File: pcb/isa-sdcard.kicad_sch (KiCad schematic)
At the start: 34 parts, among them J1 SD Card Board, J3 Bus_ISA_8bit_AB_Rev0, SW1 ADDR SEL, U10 74HC32, U12 74HC165, U13 74HC595, U14 74HC00, U2 74HC00, U22 74HCT688, U4 74HC00, U5 74HC163, U6 74HCT138, U7 74HC123, U9 74HC32, X1 16MHz

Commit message: Revising schematics and layout
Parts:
- removed C1, C25, C5: 0.1uF, Capacitor_THT:C_Disc_D5.0mm_W2.5mm_P5.00mm, symbol Device:C
- removed C20, C21: 22pF, Capacitor_THT:C_Disc_D5.0mm_W2.5mm_P5.00mm, symbol Device:C
- removed J1: SD Card Board, sdcard-holder:sdcard-socket, symbol Connector:Conn_01x06_Female
- removed R3: 10k, Resistor_THT:R_Axial_DIN0207_L6.3mm_D2.5mm_P7.62mm_Horizontal, symbol Device:R
- removed R5: 1k, Resistor_THT:R_Axial_DIN0207_L6.3mm_D2.5mm_P7.62mm_Horizontal, symbol Device:R
- removed U10, U9: 74HC32, Package_DIP:DIP-14_W7.62mm_Socket, symbol 74xx:74LS32
- removed U4: 74HC00, Package_DIP:DIP-14_W7.62mm_Socket, symbol 74xx:74HC00
- removed U6: 74HCT138, Package_DIP:DIP-16_W7.62mm_Socket, symbol 74xx:74LS138
- removed U7: 74HC123, Package_DIP:DIP-16_W7.62mm_Socket, symbol 74xx:74LS123
- added J1: SDCARD, Connector_PinSocket_2.54mm:PinSocket_1x06_P2.54mm_Vertical, symbol Connector_Generic:Conn_01x06
- added U2: 74HCT32, Package_DIP:DIP-14_W7.62mm_Socket, symbol 74xx:74LS32
- added U3: 74HCT139, Package_DIP:DIP-16_W7.62mm_Socket, symbol 74xx:74LS139
- U6: renamed from U12; value 74HC165 -> 74HCT165
- U7: renamed from U13; value 74HC595 -> 74HCT595
- renumbered C2 to C1, C24 to C10, C3 to C2, C23 to C3, C6 to C5, C7 to C6, C8 to C7, C27 to C8, C26 to C9, J3 to J2, R4 to R1, RN2 to RN1, U2 to U1, U5 to U4, U14 to U5, U22 to U8
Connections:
- net +5V is gone; now on net VCC: C1.2, C10.1, C2.2, C3.2, C4.2, C5.2, C6.2, C7.1, C8.2, C9.2, J2.B03 (VCC), J2.B29 (VCC), SW1.10, SW1.11, SW1.12, SW1.13, SW1.14, SW1.15, SW1.16, U1.14 (VCC), U4.10 (CET), U4.16 (VCC), U4.7 (CEP), U4.9 (~{PE}), U5.14 (VCC), U6.10 (DS), U6.16 (VCC), U7.10 (~{SRCLR}), U7.16 (VCC), U8.20 (VCC), X1.14 (Vcc)
- net ~{CLKSTART_DB} is gone; now on net ~{CLKSTART}: U1.5
- net A0: now also U3.14 (A0), U3.2 (A0)
- net A1: now also U3.13 (A1), U3.3 (A1)
- net A2: now also U8.2 (P0)
- net A3: now also U8.4 (P1); no longer U8.2 (P0)
- net A4: now also U8.6 (P2); no longer U8.4 (P1)
- net A5: now also U8.8 (P3); no longer U8.6 (P2)
- net A6: now also U8.11 (P4); no longer U8.8 (P3)
- net A7: now also U8.13 (P5); no longer U8.11 (P4)
- net A8: now also U8.15 (P6); no longer U8.13 (P5)
- net A9: now also U8.17 (P7); no longer U8.15 (P6)
- net CLK: now also J1.2 (Pin_2)
- net GND: now also J1.6 (Pin_6), U2.10, U2.12, U2.13, U2.7 (GND), U2.9, U3.8 (GND); no longer U8.17 (P7), U8.18 (R7)
- net MISO: now also J1.4 (Pin_4)
- net MOSI: now also J1.3 (Pin_3)
- net ~{CLKSTART}: now also U3.11 (O1)
- net ~{CS}: now also J1.1 (Pin_1)
- net ~{PORTSEL}: now also U2.1, U2.4
- net ~{RD}: now also U2.2
- net ~{SDCS_RESET}: now also U3.7 (O3)
- net ~{SDCS_SET}: now also U3.6 (O2)
- net ~{SDOUT_RESET}: now also U3.9 (O3)
- net ~{SDOUT_SET}: now also U3.10 (O2)
- net ~{SER_RD}: now also U3.4 (O0)
- net ~{SER_WR}: now also U3.12 (O0)
- net ~{WR}: now also U2.5
- net at RN1.8 (R7), U8.16 (R6): now also SW1.2; no longer SW1.1
- net at RN1.7 (R6), U8.14 (R5): now also SW1.3; no longer SW1.2
- net at RN1.6 (R5), U8.12 (R4): now also SW1.4; no longer SW1.3
- net at RN1.5 (R4), U8.9 (R3): now also SW1.5; no longer SW1.4
- net at RN1.4 (R3), U8.7 (R2): now also SW1.6; no longer SW1.5
- net at RN1.3 (R2), U8.5 (R1): now also SW1.7; no longer SW1.6
- net at RN1.2 (R1), U8.3 (R0): now also SW1.8; no longer SW1.7
- net VCC: now reaches SW1.9
- net VCC: now also J1.5 (Pin_5), U2.14 (VCC), U3.16 (VCC)
- net at RN1.9 (R8): now also SW1.1, U8.18 (R7)
- net RESET: no longer names the net of J2.B02 (RESET)
- net SD_SPI: no longer names the net of U1.2, U1.6, U4.1 (~{MR})
- new net: U2.6, U3.15 (E)
- new net: U2.3, U3.1 (E)
- no-connect marks 61 -> 44
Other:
- note removed: "10k resistor with 22pF cap gives t = 0.45RC = 0.1us delay between consecutive pulses"
- note removed: "1k resistor with 22pF cap gives 0.45*RC = 0.01us active low pulse"
- note removed: "MULTIVIBRATOR DELAY COMPONENT"
- note removed: "SD card"
- note removed: "in $42"
- note removed: "in $43"
- note removed: "out $42"
- note removed: "out $43"
- title: Philips P2000T SD-CARD SLOT2 cartridge -> ISA-TO-SDCARD
- moved on the sheet: SW1

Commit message: Revising design
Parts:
- added J3: Conn_01x05_Pin, Connector_PinHeader_2.54mm:PinHeader_1x05_P2.54mm_Vertical, symbol Connector:Conn_01x05_Pin
- added TP1: ~{CS}, TestPoint:TestPoint_Loop_D3.80mm_Drill2.0mm, symbol Connector:TestPoint_Probe
- added TP2: CLK, TestPoint:TestPoint_Loop_D3.80mm_Drill2.0mm, symbol Connector:TestPoint_Probe
- added TP3: MOSI, TestPoint:TestPoint_Loop_D3.80mm_Drill2.0mm, symbol Connector:TestPoint_Probe
- added TP4, TP5: MISO, TestPoint:TestPoint_Loop_D3.80mm_Drill2.0mm, symbol Connector:TestPoint_Probe
- J1: footprint Connector_PinSocket_2.54mm:PinSocket_1x06_P2.54mm_Vertical -> sdcard-holder:sdcard-socket
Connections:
- net CLK: now also J3.2 (Pin_2), TP2.1
- net GND: now also J3.5 (Pin_5), TP5.1
- net MISO: now also J3.4 (Pin_4), TP4.1
- net MOSI: now also J3.3 (Pin_3), TP3.1
- net ~{CS}: now also J3.1 (Pin_1), TP1.1

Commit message: Revising lay-out
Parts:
- added C11: 0.1uF, Capacitor_THT:C_Disc_D5.0mm_W2.5mm_P5.00mm, symbol Device:C
- added H1, H2: MountingHole_Pad, MountingHole:MountingHole_3.2mm_M3_DIN965_Pad_TopBottom, symbol Mechanical:MountingHole_Pad
- added U9: 74HCT245, Package_DIP:DIP-20_W7.62mm_Socket, symbol 74xx:74HC245
- U6: value 74HCT165 -> 74HC165
- U7: value 74HCT595 -> 74HC595
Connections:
- net D0: now also U9.18 (B0); no longer J2.A09 (DB0)
- net D1: now also U9.17 (B1); no longer J2.A08 (DB1)
- net D2: now also U9.16 (B2); no longer J2.A07 (DB2)
- net D3: now also U9.15 (B3); no longer J2.A06 (DB3)
- net D4: now also U9.14 (B4); no longer J2.A05 (DB4)
- net D5: now also U9.13 (B5); no longer J2.A04 (DB5)
- net D6: now also U9.12 (B6); no longer J2.A03 (DB6)
- net D7: now also U9.11 (B7); no longer J2.A02 (DB7)
- net GND: now also C11.1, H1.1, H2.1, U9.10 (GND)
- net VCC: now also C11.2, U9.20 (VCC)
- net ~{PORTSEL}: now also U9.19 (CE)
- net ~{SER_RD}: now also U9.1 (A->B)
- new net DB0: J2.A09 (DB0), U9.2 (A0)
- new net DB1: J2.A08 (DB1), U9.3 (A1)
- new net DB2: J2.A07 (DB2), U9.4 (A2)
- new net DB3: J2.A06 (DB3), U9.5 (A3)
- new net DB4: J2.A05 (DB4), U9.6 (A4)
- new net DB5: J2.A04 (DB5), U9.7 (A5)
- new net DB6: J2.A03 (DB6), U9.8 (A6)
- new net DB7: J2.A02 (DB7), U9.9 (A7)
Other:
- note added: "Buffers data bus and ensures voltage translation between LS and HC chips."

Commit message: Expanding PCB and adding reading directory to firmware
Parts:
- removed J3: Conn_01x05_Pin, Connector_PinHeader_2.54mm:PinHeader_1x05_P2.54mm_Vertical, symbol Connector:Conn_01x05_Pin
- removed TP5: MISO, TestPoint:TestPoint_Loop_D3.80mm_Drill2.0mm, symbol Connector:TestPoint_Probe
- added C12, C13: 0.1uF, Capacitor_THT:C_Disc_D5.0mm_W2.5mm_P5.00mm, symbol Device:C
- added D1, D2, D3: LED, LED_THT:LED_D5.0mm, symbol Device:LED
- added TP6: ~{Q}, TestPoint:TestPoint_Loop_D2.54mm_Drill1.5mm_Beaded, symbol Connector:TestPoint_Probe
- added U10: 74HC74, Package_DIP:DIP-14_W7.62mm_Socket, symbol 74xx:74HC74
- added U11: 74HC08, Package_DIP:DIP-14_W7.62mm_Socket, symbol 74xx:74LS08
- added U12: 74HC04, Package_DIP:DIP-14_W7.62mm_Socket, symbol 74xx:74HC04
- TP1, TP2, TP3, TP4: footprint TestPoint:TestPoint_Loop_D3.80mm_Drill2.0mm -> TestPoint:TestPoint_Loop_D2.54mm_Drill1.5mm_Beaded
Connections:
- net 16MHz: now also U10.11 (C), U10.3 (C)
- net GND: now also C12.1, C13.1, D1.1 (K), U10.7 (GND), U11.12, U11.13, U11.7 (GND), U12.7 (GND)
- net MISO: now also U12.13
- net MOSI: now also U12.9
- net VCC: now also C12.2, C13.2, D2.2 (A), D3.2 (A), U10.1 (~{R}), U10.10 (~{S}), U10.13 (~{R}), U10.14 (VCC), U10.4 (~{S}), U11.14 (VCC), U12.14 (VCC)
- net ~{CLKSTART}: now also U11.3; no longer U3.11 (O1)
- net ~{CS}: now also U12.3
- net ~{SER_RD}: now also U11.6; no longer U3.4 (O0)
- net ~{SER_RD_AND_PULSE}: now reaches U3.5 (O1)
- net ~{SER_RD_AND_PULSE}: now also U10.2 (D), U11.10, U11.5
- new net: D1.2 (A), U12.4
- new net: U10.12 (D), U10.5 (Q)
- new net: TP6.1, U10.8 (~{Q}), U11.9
- new net: U11.8, U12.1
- new net: U11.2, U12.2
- new net: D2.1 (K), U12.10
- new net: U12.11, U12.8
- new net: D3.1 (K), U12.6
- new net: U12.12, U12.5
- new net ~{PULSE}: U11.1, U3.11 (O1)
- new net ~{RQ_SER_RD}: U11.4, U3.4 (O0)
- no-connect marks 44 -> 46
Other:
- note added: "First read, then pulse, so another byte is made ready. Used for reading blocks."
- note added: "in $XX0: ~{SER_RD} is pulled low, reading from the in register. in $XX1: Does READ and then PULSE in $XX2: ~{SDOUT_SET} is pulled low, pulling MISO low via a 10k resistor. in $XX3: ~{SDOUT_RESET} is pulled low, pulling MISO high via a 10k resistor. When no card is present, the output of the SD card will follow the output of the SET/RESET latch, however if a card is present, though unresponsive, i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"
- note removed: "in $XX0: ~{SER_RD} is pulled low, reading from the in register. in $XX1: Does nothing in $XX2: ~{SDOUT_SET} is pulled low, pulling MISO low via a 10k resistor. in $XX3: ~{SDOUT_RESET} is pulled low, pulling MISO high via a 10k resistor. When no card is present, the output of the SD card will follow the output of the SET/RESET latch, however if a card is present, though unresponsive, it will not f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"
- moved on the sheet: C1, C11, C2, C4, C5, C7, J1, TP1, TP2, TP3, TP4, U1E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

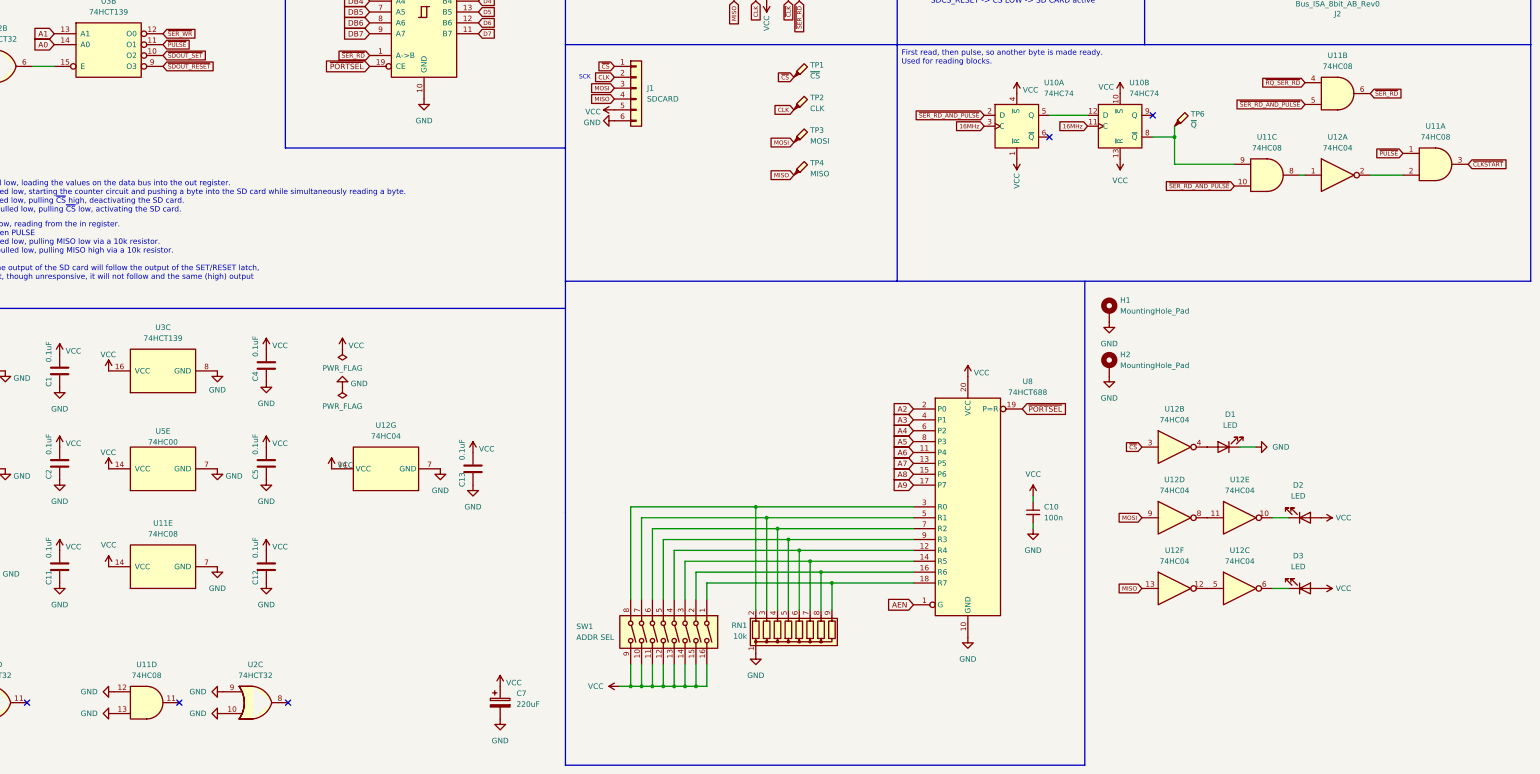
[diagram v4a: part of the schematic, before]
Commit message: Adding immediate pulse after rwrite and optional pulse after read
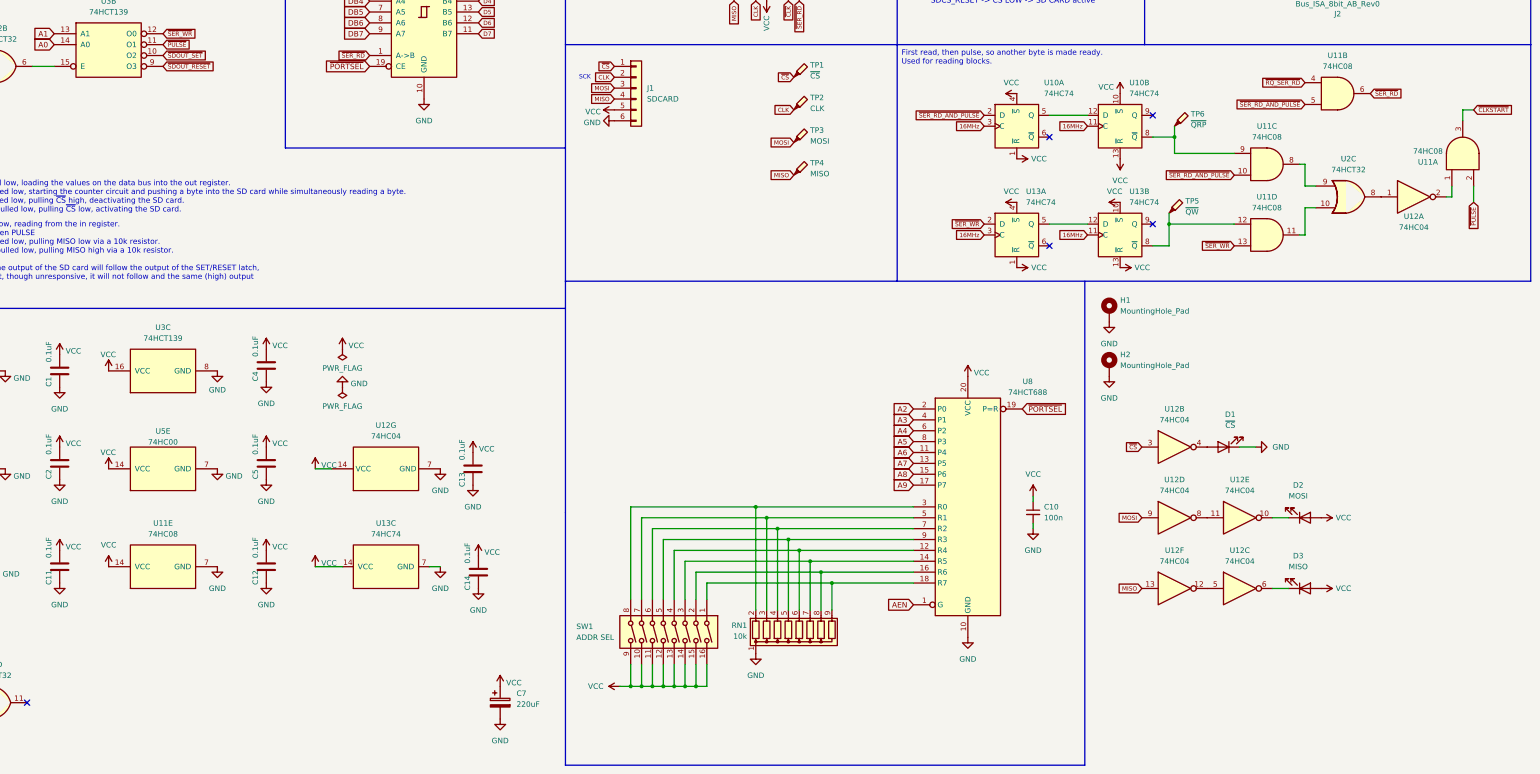
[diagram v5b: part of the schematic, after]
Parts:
- added C14: 0.1uF, Capacitor_THT:C_Disc_D5.0mm_W2.5mm_P5.00mm, symbol Device:C
- added TP5: ~{QW}, TestPoint:TestPoint_Loop_D2.54mm_Drill1.5mm_Beaded, symbol Connector:TestPoint_Probe
- added U13: 74HC74, Package_DIP:DIP-14_W7.62mm_Socket, symbol 74xx:74HC74
- D1: value LED -> ~{CS}
- D2: value LED -> MOSI
- D3: value LED -> MISO
- TP6: value ~{Q} -> ~{QRP}
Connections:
- net 16MHz: now also U13.11 (C), U13.3 (C)
- net GND: now also C14.1, U13.7 (GND); no longer U11.12, U11.13, U2.10, U2.9
- net VCC: now also C14.2, U13.1 (~{R}), U13.10 (~{S}), U13.13 (~{R}), U13.14 (VCC), U13.4 (~{S})
- net ~{PULSE}: now also U11.2; no longer U11.1
- net ~{SER_WR}: now also U11.13, U13.2 (D)
- net at U12.1: now also U2.8; no longer U11.8
- net at U12.2: now also U11.1; no longer U11.2
- net at U11.11: now also U2.10
- new net: U13.12 (D), U13.5 (Q)
- new net: TP5.1, U11.12, U13.8 (~{Q})
- new net: U11.8, U2.9
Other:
- moved on the sheet: U11A, U11C, U11D, U12A, U2C
